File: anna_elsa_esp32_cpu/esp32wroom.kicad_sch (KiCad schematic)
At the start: 25 parts, among them J12 HEADER_6x2, Q4 BSS138, Q7 BSS138, SW1 RESET, SW2 BOOT, U1 ESP32-WROOM-32E(16M), U10 SN74LVC1G17, U11 SN74LVC1G17, U2 SN74LVC1G17, U5 SN74LVC1G17, U6 SN74LVC1G17, U7 SN74LVC1G17, U9 SN74LVC1G17

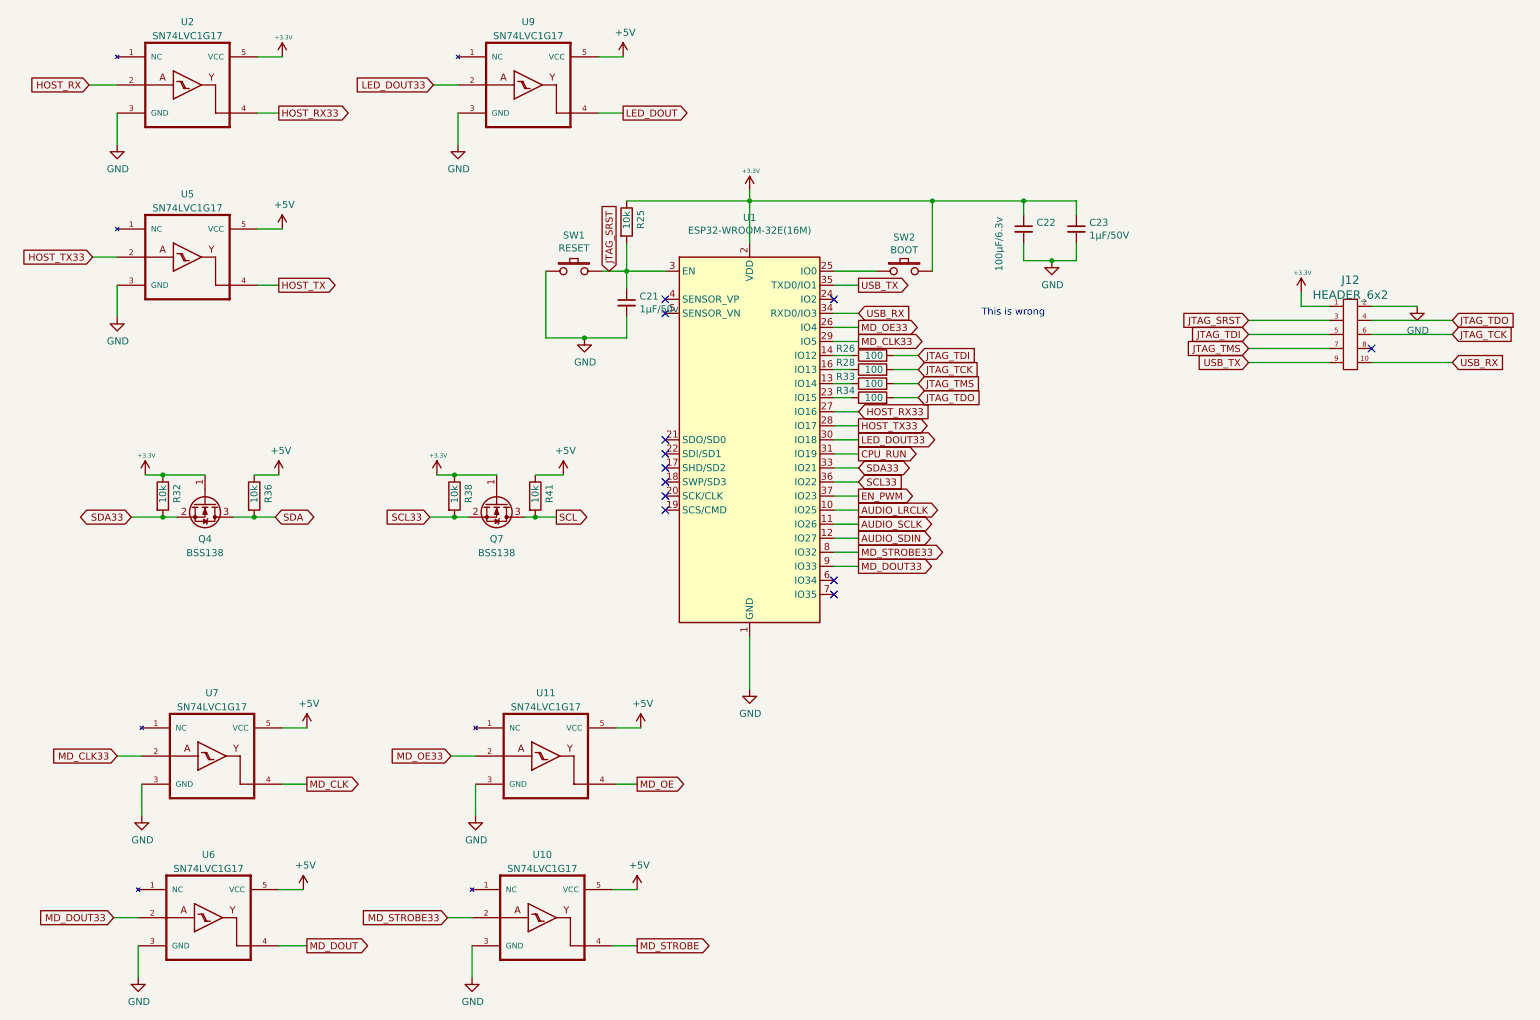
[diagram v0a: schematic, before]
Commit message: Added current cpu pcb and removed old
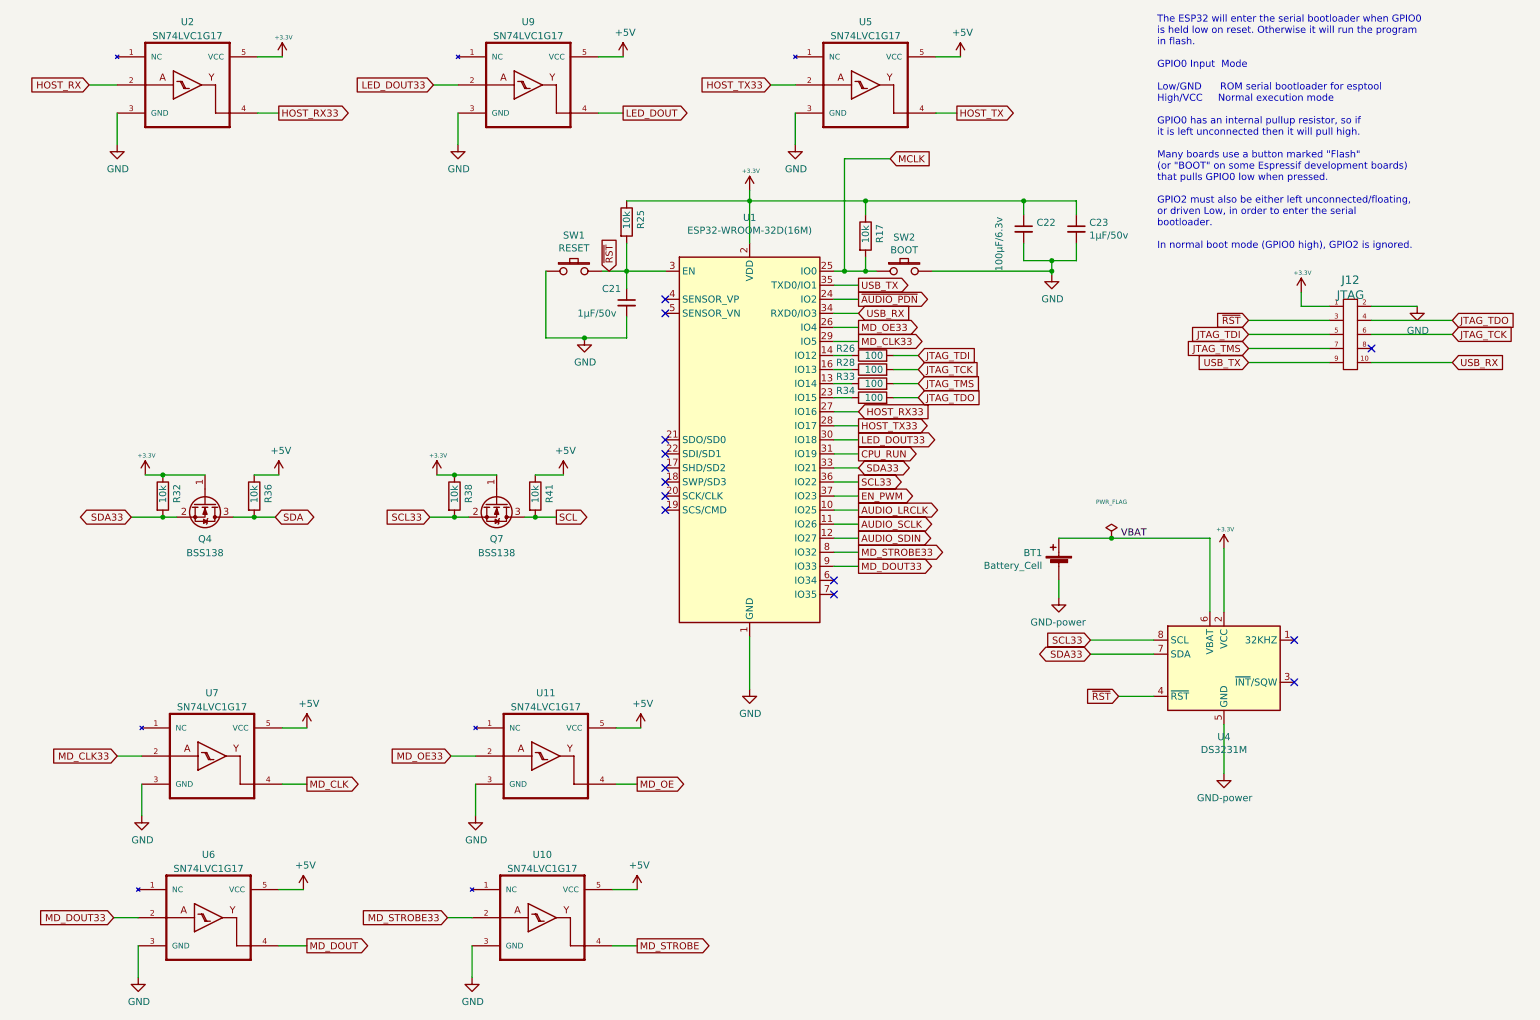
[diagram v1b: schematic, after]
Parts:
- added BT1: Battery_Cell, Battery:BatteryHolder_Keystone_1060_1x2032, symbol Device:Battery_Cell
- added R17: 10k, Resistor_SMD:R_0603_1608Metric, symbol Device:R
- added U4: DS3231M, Package_SO:SOIC-8_3.9x4.9mm_P1.27mm, symbol Timer_RTC:DS3231MZ
- C21: MPN (none) -> CL21B105KBFNNNE; Manufacturer (none) -> Samsung Electro-Mechanics
- C22: MPN (none) -> CL31A107MQHNNNE; Manufacturer (none) -> Samsung Electro-Mechanics
- C23: value 1µF/50V -> 1µF/50v; MPN (none) -> CL21B105KBFNNNE; Manufacturer (none) -> Samsung Electro-Mechanics
- J12: value HEADER_6x2 -> JTAG; Manufacturer (none) -> BOOMELE(Boom Precision Elec)
- Q4, Q7: MPN (none) -> BSS138L; Manufacturer (none) -> onsemi
- R25, R32, R36, R38, R41: LCSC C17477 -> C25804; MPN (none) -> 0603WAF1002T5E; Manufacturer (none) -> UNI-ROYAL(Uniroyal Elec)
- R26, R28, R33, R34: MPN (none) -> 0603WAF1000T5E
- U1: value ESP32-WROOM-32E(16M) -> ESP32-WROOM-32D(16M); JLC QFN-38_EP_18.0x25.5x1.27P -> SMD38,18x25.5x3.1; LCSC C701343 -> C529578; MPN ESP32-WROOM-32E(16MB) -> ESP32-WROOM-32D(16MB)
- U10, U11, U5, U6: footprint Package_TO_SOT_SMD:SOT-23-5 -> Package_TO_SOT_SMD:SOT-353_SC-70-5; JLC SOT-23-5 -> C10425; LCSC C7836 -> C10425; MPN SN74LVC1G17QDBVRQ1 -> (none)
- U2: footprint Package_TO_SOT_SMD:SOT-23-5 -> Package_TO_SOT_SMD:SOT-353_SC-70-5; JLC SOT-23-5 -> C10425; LCSC C7836 -> C10425; MPN SN74LVC1G17QDBVRQ1 -> SN74LVC1G17DCKR
- U7: footprint Package_TO_SOT_SMD:SOT-23-5 -> Package_TO_SOT_SMD:SOT-353_SC-70-5; JLC SOT-23-5 -> C10425; LCSC C7836 -> C10425
- U9: footprint Package_TO_SOT_SMD:SOT-23-5 -> Package_TO_SOT_SMD:SOT-353_SC-70-5; JLC SOT-23-5 -> C10425; LCSC C7836 -> C10425; MPN SN74LVC1G17QDBVRQ1 -> SN74LVC1G17QDBVRQ
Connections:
- net GND: now also SW2.2, BT1.2 (-), U4.5 (GND)
- net SCL33: now also U4.8 (SCL)
- net SDA33: now also U4.7 (SDA)
- net ~{AUDIO_PDN}: now reaches U1.24 (IO2)
- net MCLK: now reaches SW2.1, U1.25 (IO0)
- net MCLK: now also R17.2
- net +3V3 renamed +3.3V
- net +3.3V: now also R17.1, U4.2 (VCC); no longer SW2.2
- net JTAG_SRST renamed ~{RST}
- net ~{RST}: now also U4.4 (~{RST})
- new net VBAT: BT1.1 (+), U4.6 (VBAT)
- no-connect marks 12 -> 13
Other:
- note added: "The ESP32 will enter the serial bootloader when GPIO0 is held low on reset. Otherwise it will run the program in flash. GPIO0 Input Mode Low/GND ROM serial bootloader for esptool High/VCC Normal execution mode GPIO0 has an internal pullup resistor, so if it is left unconnected then it will pull high. Many boards use a button marked "Flash" (or "BOOT" on some Espressif development boards) that pul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"
- note removed: "This is wrong"
- moved on the sheet: U5

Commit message: Latest schematics
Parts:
- R32, R36, R38, R41: value 10k -> 4k7; LCSC C25804 -> C123022; MPN 0603WAF1002T5E -> MCR03EZPJ472; Manufacturer UNI-ROYAL(Uniroyal Elec) -> ROHM Semicon
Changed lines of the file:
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@@
       (effects (font (size 1.27 1.27)) (justify left))
     )
-    (property "Value" "10k" (id 1) (at 54.61 102.87 90)
+    (property "Value" "4k7" (id 1) (at 54.61 102.87 90)
       (effects (font (size 1.27 1.27)) (justify left))
     )
@@
       (effects (font (size 1.27 1.27)) hide)
     )
-    (property "LCSC" "C25804" (id 4) (at 54.61 101.6 90)
+    (property "LCSC" "C123022" (id 4) (at 54.61 101.6 90)
       (effects (font (size 1.27 1.27)) hide)
     )
@@
       (effects (font (size 1.27 1.27)) hide)
     )
-    (property "MPN" "0603WAF1002T5E" (id 7) (at 54.61 101.6 0)
-      (effects (font (size 1.27 1.27)) hide)
-    )
-    (property "Manufacturer" "UNI-ROYAL(Uniroyal Elec)" (id 8) (at 54.61 101.6 0)
+    (property "MPN" "MCR03EZPJ472" (id 7) (at 54.61 101.6 0)
+      (effects (font (size 1.27 1.27)) hide)
+    )
+    (property "Manufacturer" "ROHM Semicon" (id 8) (at 54.61 101.6 0)
       (effects (font (size 1.27 1.27)) hide)
     )
@@
       (effects (font (size 1.27 1.27)) (justify left))
     )
-    (property "Value" "10k" (id 1) (at 38.1 102.87 90)
+    (property "Value" "4k7" (id 1) (at 38.1 102.87 90)
       (effects (font (size 1.27 1.27)) (justify left))
     )
@@
       (effects (font (size 1.27 1.27)) hide)
     )
-    (property "LCSC" "C25804" (id 4) (at 38.1 101.6 90)
+    (property "LCSC" "C123022" (id 4) (at 38.1 101.6 90)
       (effects (font (size 1.27 1.27)) hide)
     )
@@
       (effects (font (size 1.27 1.27)) hide)
     )
-    (property "MPN" "0603WAF1002T5E" (id 7) (at 38.1 101.6 0)
-      (effects (font (size 1.27 1.27)) hide)
-    )
-    (property "Manufacturer" "UNI-ROYAL(Uniroyal Elec)" (id 8) (at 38.1 101.6 0)
+    (property "MPN" "MCR03EZPJ472" (id 7) (at 38.1 101.6 0)
+      (effects (font (size 1.27 1.27)) hide)
+    )
+    (property "Manufacturer" "ROHM Semicon" (id 8) (at 38.1 101.6 0)
       (effects (font (size 1.27 1.27)) hide)
     )
@@
       (effects (font (size 1.27 1.27)) (justify left))
     )
-    (property "Value" "10k" (id 1) (at 90.805 102.87 90)
+    (property "Value" "4k7" (id 1) (at 90.805 102.87 90)
       (effects (font (size 1.27 1.27)) (justify left))
     )
@@
       (effects (font (size 1.27 1.27)) hide)
     )
-    (property "Datasheet" "~" (id 3) (at 90.805 101.6 0)
-      (effects (font (size 1.27 1.27)) hide)
-    )
-    (property "LCSC" "C25804" (id 4) (at 90.805 101.6 90)
+    (property "Datasheet" "https://datasheet.lcsc.com/lcsc/1912111437_ROHM-Semicon-MCR03EZPJ472_C123022.pdf" (id 3) (at 90.805 101.6 0)
+      (effects (font (size 1.27 1.27)) hide)
+    )
+    (property "LCSC" "C123022" (id 4) (at 90.805 101.6 90)
       (effects (font (size 1.27 1.27)) hide)
     )
@@
       (effects (font (size 1.27 1.27)) hide)
     )
-    (property "MPN" "0603WAF1002T5E" (id 7) (at 90.805 101.6 0)
-      (effects (font (size 1.27 1.27)) hide)
-    )
-    (property "Manufacturer" "UNI-ROYAL(Uniroyal Elec)" (id 8) (at 90.805 101.6 0)
+    (property "MPN" "MCR03EZPJ472" (id 7) (at 90.805 101.6 0)
+      (effects (font (size 1.27 1.27)) hide)
+    )
+    (property "Manufacturer" "ROHM Semicon" (id 8) (at 90.805 101.6 0)
       (effects (font (size 1.27 1.27)) hide)
     )
@@
       (effects (font (size 1.27 1.27)) (justify left))
     )
-    (property "Value" "10k" (id 1) (at 105.41 102.87 90)
+    (property "Value" "4k7" (id 1) (at 105.41 102.87 90)
       (effects (font (size 1.27 1.27)) (justify left))
     )
@@
       (effects (font (size 1.27 1.27)) hide)
     )
-    (property "LCSC" "C25804" (id 4) (at 105.41 101.6 90)
+    (property "LCSC" "C123022" (id 4) (at 105.41 101.6 90)
       (effects (font (size 1.27 1.27)) hide)
     )
@@
       (effects (font (size 1.27 1.27)) hide)
     )
-    (property "MPN" "0603WAF1002T5E" (id 7) (at 105.41 101.6 0)
-      (effects (font (size 1.27 1.27)) hide)
-    )
-    (property "Manufacturer" "UNI-ROYAL(Uniroyal Elec)" (id 8) (at 105.41 101.6 0)
-      (effects (font (size 1.27 1.27)) hide)
-    )
+    (property "MPN" "MCR03EZPJ472" (id 7) (at 105.41 101.6 0)
+      (effects (font (size 1.27 1.27)) hide)
+    )
+    (property "Manufacturer" "ROHM Semicon" (id 8) (at 105.41 101.6 0)
+      (effects (font (size 1.27 1.27)) hide)
+    )
